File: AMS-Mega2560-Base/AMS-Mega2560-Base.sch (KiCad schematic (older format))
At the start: 18 parts, among them J23 RTD1, J24 RTD2, J25 Sense, J26 AdafruitUltimateGPS, J27 Sense, P1 Digital, P10 CONN_01X01, P11 CONN_01X01, P12 CONN_01X01, P13 CONN_01X01, P2 Power, P3 Analog, P4 Analog, P5 PWM, P6 PWM, P7 Communication, P8 CONN_01X01, P9 CONN_01X01

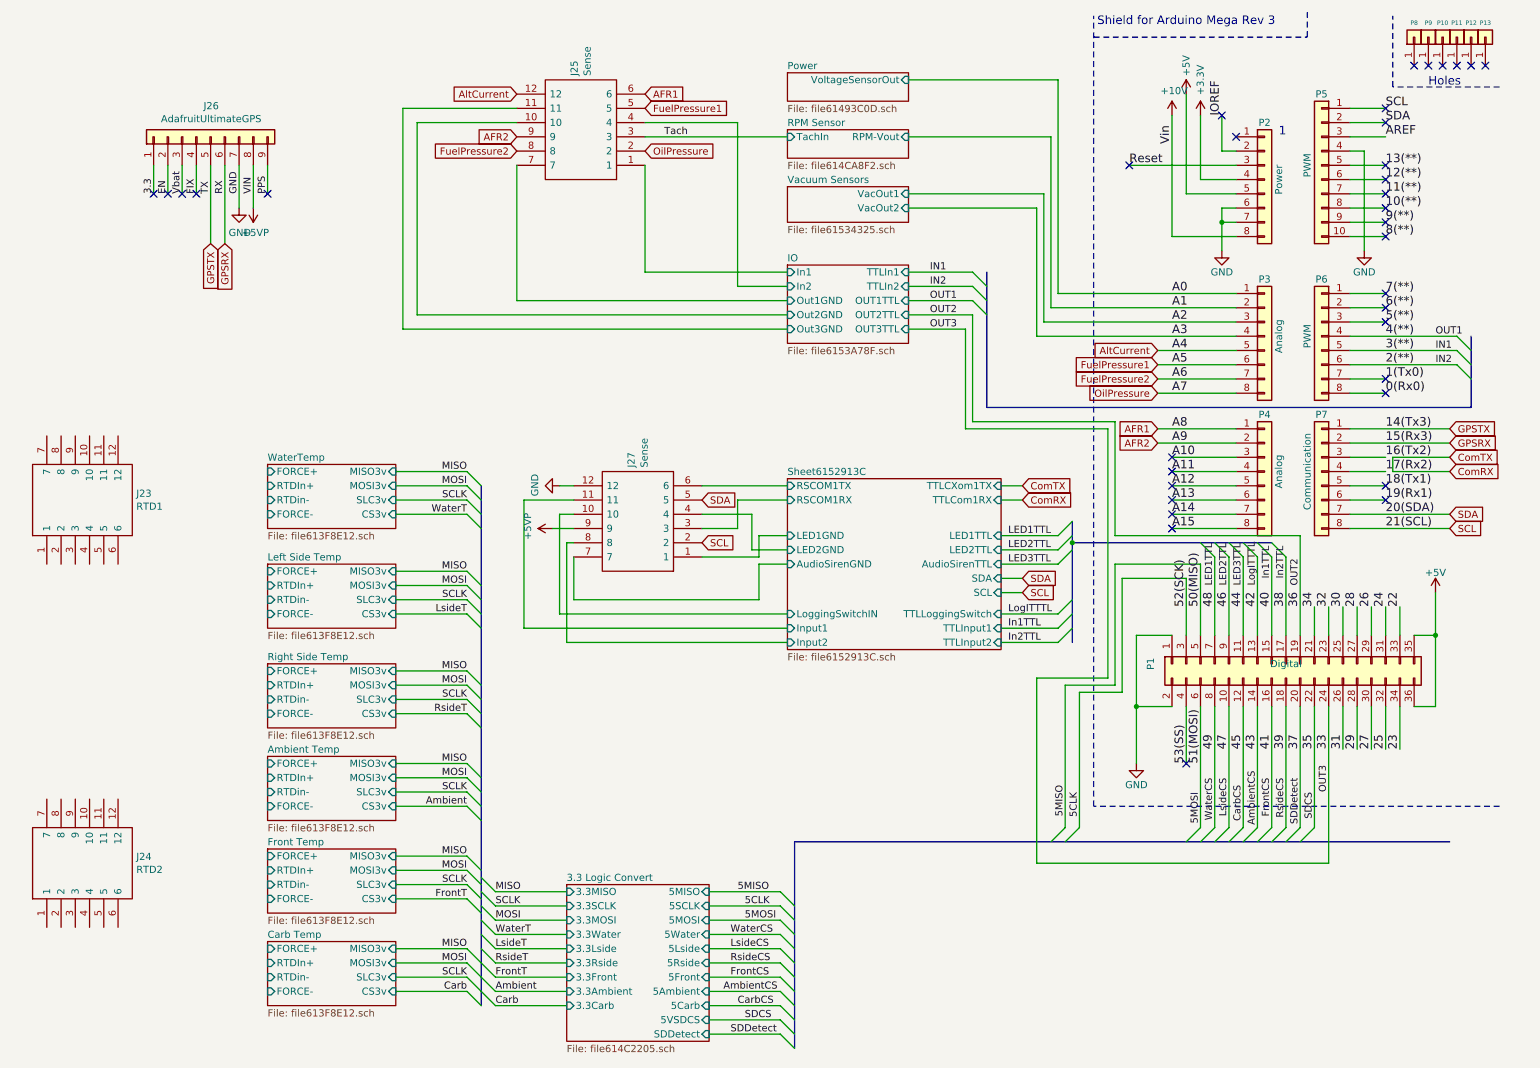
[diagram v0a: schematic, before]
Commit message: fixed the schematics for the RTC, IO and COMs. Realigned the RTD to screw term. need to finish the 3.3v portion of the power systems.
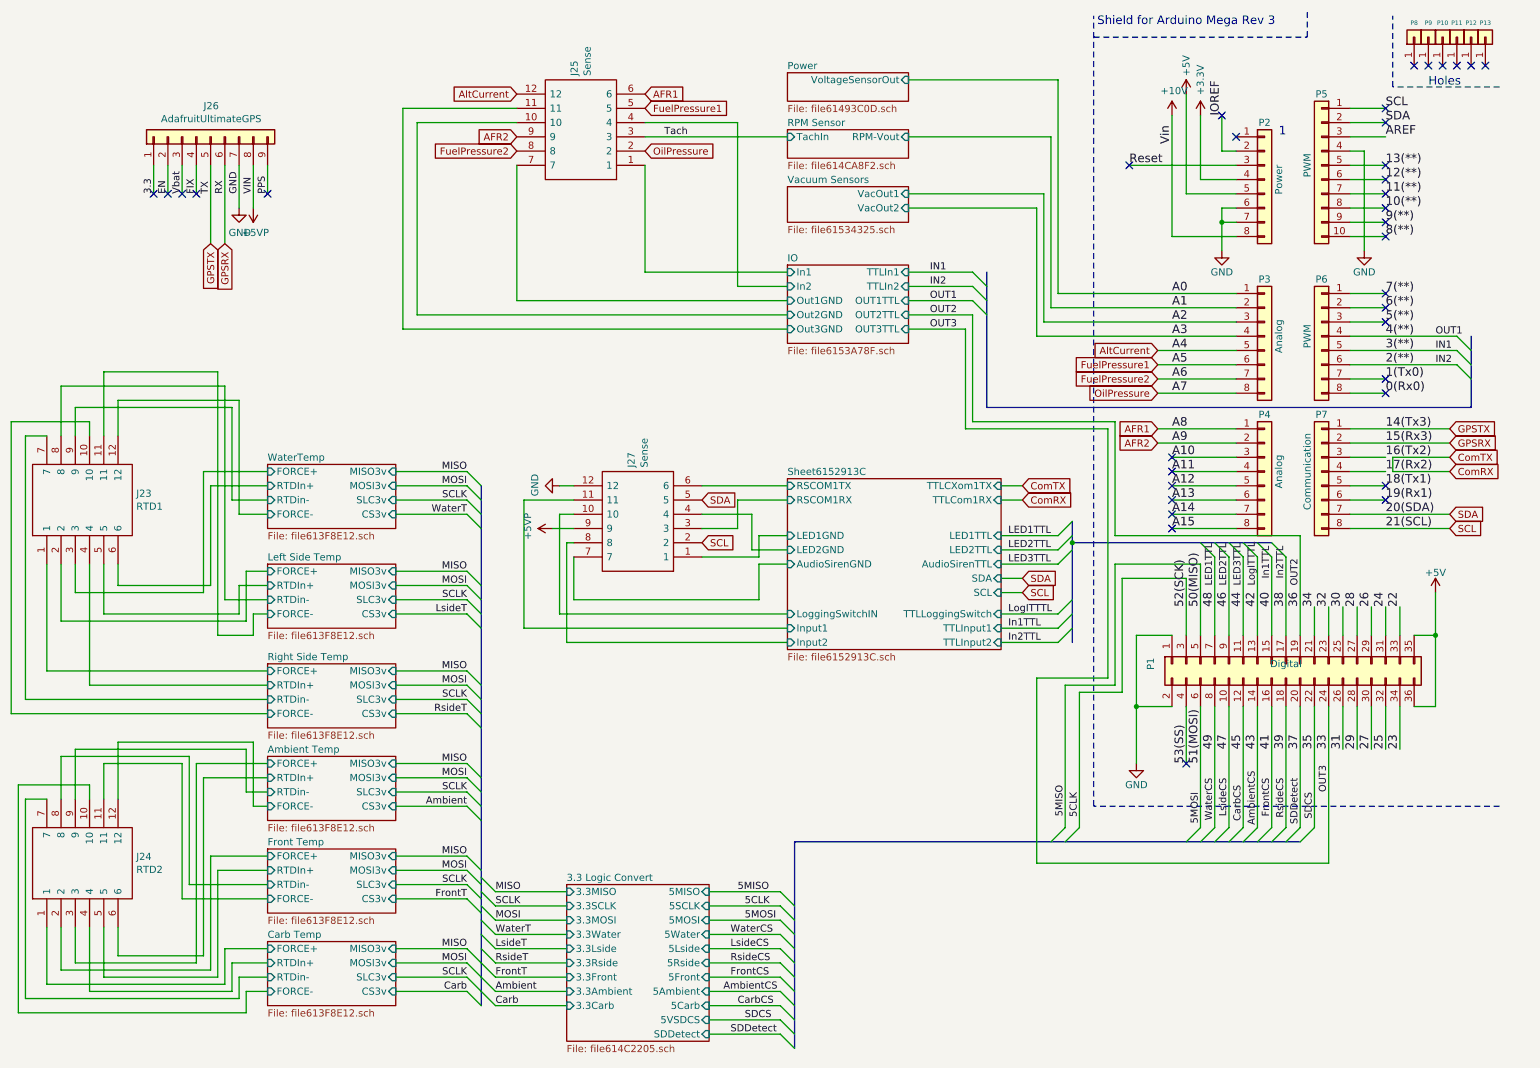
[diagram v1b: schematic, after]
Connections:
- net Ambient Temp/FORCE+: now also J24.3
- net Ambient Temp/FORCE-: now also J24.12
- net Ambient Temp/RTDIn+: now also J24.6
- net Ambient Temp/RTDin-: now also J24.9
- net Carb Temp/FORCE+: now also J24.1
- net Carb Temp/FORCE-: now also J24.10
- net Carb Temp/RTDIn+: now also J24.4
- net Carb Temp/RTDin-: now also J24.7
- net Front Temp/FORCE+: now also J24.2
- net Front Temp/FORCE-: now also J24.11
- net Front Temp/RTDIn+: now also J24.5
- net Front Temp/RTDin-: now also J24.8
- net Left Side Temp/FORCE+: now also J23.2
- net Left Side Temp/FORCE-: now also J23.11
- net Left Side Temp/RTDIn+: now also J23.5
- net Left Side Temp/RTDin-: now also J23.8
- net Right Side Temp/FORCE+: now also J23.1
- net Right Side Temp/FORCE-: now also J23.10
- net Right Side Temp/RTDIn+: now also J23.4
- net Right Side Temp/RTDin-: now also J23.7
- net WaterTemp/FORCE+: now also J23.3
- net WaterTemp/FORCE-: now also J23.12
- net WaterTemp/RTDIn+: now also J23.6
- net WaterTemp/RTDin-: now also J23.9
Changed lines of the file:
@@
 Text Label 10000 5950 1    50   ~ 0
 OUT3
-Wire Bus Line
-	8200 4050 8200 4200
-Wire Bus Line
-	11000 2750 11000 3250
-Wire Bus Line
-	7600 2300 7600 3250
-Wire Bus Line
-	8200 4200 8200 4900
-Wire Bus Line
-	8200 4200 9600 4200
-Wire Bus Line
-	6250 6300 6250 7750
-Wire Bus Line
-	6250 6300 10850 6300
-Wire Bus Line
-	4050 3800 4050 7450
 $Sheet
 S 6200 3750 1500 1200
@@
 F19 "LoggingSwitchIN" I L 6200 4700 50
 $EndSheet
+Wire Wire Line
+	2550 3700 2100 3700
+Wire Wire Line
+	2100 3700 2100 4550
+Wire Wire Line
+	2100 4550 1200 4550
+Wire Wire Line
+	1200 4550 1200 4350
+Wire Wire Line
+	2550 3800 2150 3800
+Wire Wire Line
+	2150 3800 2150 4500
+Wire Wire Line
+	2150 4500 1500 4500
+Wire Wire Line
+	1500 4500 1500 4350
+Wire Wire Line
+	2550 3900 2300 3900
+Wire Wire Line
+	2300 3250 1200 3250
+Wire Wire Line
+	1200 3250 1200 3450
+Wire Wire Line
+	2550 4000 2350 4000
+Wire Wire Line
+	2350 4000 2350 3200
+Wire Wire Line
+	2350 3200 1500 3200
+Wire Wire Line
+	1500 3200 1500 3450
+Wire Wire Line
+	2550 4400 2400 4400
+Wire Wire Line
+	2400 4400 2400 4750
+Wire Wire Line
+	2400 4750 1100 4750
+Wire Wire Line
+	1100 4750 1100 4350
+Wire Wire Line
+	2550 4500 2350 4500
+Wire Wire Line
+	2350 4500 2350 4700
+Wire Wire Line
+	1400 4700 1400 4350
+Wire Wire Line
+	2300 3900 2300 3250
+Wire Wire Line
+	1100 3450 1100 3100
+Wire Wire Line
+	1100 3100 2250 3100
+Wire Wire Line
+	2250 3100 2250 4600
+Wire Wire Line
+	2250 4600 2550 4600
+Wire Wire Line
+	2350 4700 1400 4700
+Wire Wire Line
+	2550 4700 2450 4700
+Wire Wire Line
+	2450 4700 2450 4850
+Wire Wire Line
+	2450 4850 2200 4850
+Wire Wire Line
+	2200 4850 2200 3000
+Wire Wire Line
+	2200 3000 1400 3000
+Wire Wire Line
+	1400 3000 1400 3450
+Wire Wire Line
+	2550 5100 1000 5100
+Wire Wire Line
+	1000 5100 1000 4350
+Wire Wire Line
+	2550 5200 1300 5200
+Wire Wire Line
+	1300 5200 1300 4350
+Wire Wire Line
+	2550 5300 850  5300
+Wire Wire Line
+	850  5300 850  3450
+Wire Wire Line
+	850  3450 1000 3450
+Wire Wire Line
+	1300 3450 1300 3350
+Wire Wire Line
+	1300 3350 750  3350
+Wire Wire Line
+	750  3350 750  5400
+Wire Wire Line
+	750  5400 2550 5400
+Wire Wire Line
+	1200 6900 1200 7150
+Wire Wire Line
+	1200 7150 2050 7150
+Wire Wire Line
+	2050 7150 2050 5750
+Wire Wire Line
+	2050 5750 2550 5750
+Wire Wire Line
+	2550 5850 2100 5850
+Wire Wire Line
+	2100 5850 2100 7100
+Wire Wire Line
+	2100 7100 1500 7100
+Wire Wire Line
+	1500 7100 1500 6900
+Wire Wire Line
+	1200 6000 1200 5650
+Wire Wire Line
+	1200 5650 2400 5650
+Wire Wire Line
+	2400 5650 2400 5950
+Wire Wire Line
+	2400 5950 2550 5950
+Wire Wire Line
+	1500 6000 1500 5600
+Wire Wire Line
+	1500 5600 2450 5600
+Wire Wire Line
+	2450 5600 2450 6050
+Wire Wire Line
+	2450 6050 2550 6050
+Wire Wire Line
+	2550 6400 2150 6400
+Wire Wire Line
+	2150 6400 2150 7200
+Wire Wire Line
+	2150 7200 1100 7200
+Wire Wire Line
+	1100 7200 1100 6900
+Wire Wire Line
+	1400 6900 1400 7250
+Wire Wire Line
+	1400 7250 2200 7250
+Wire Wire Line
+	2200 7250 2200 6500
+Wire Wire Line
+	2200 6500 2550 6500
+Wire Wire Line
+	1100 6000 1100 5700
+Wire Wire Line
+	1100 5700 2000 5700
+Wire Wire Line
+	2000 5700 2000 6600
+Wire Wire Line
+	2000 6600 2550 6600
+Wire Wire Line
+	2550 6700 1950 6700
+Wire Wire Line
+	1950 6700 1950 5750
+Wire Wire Line
+	1950 5750 1400 5750
+Wire Wire Line
+	1400 5750 1400 6000
+Wire Wire Line
+	2550 7050 2250 7050
+Wire Wire Line
+	1000 7300 1000 6900
+Wire Wire Line
+	2250 7050 2250 7300
+Wire Wire Line
+	2250 7300 1000 7300
+Wire Wire Line
+	1300 6900 1300 7350
+Wire Wire Line
+	1300 7350 2300 7350
+Wire Wire Line
+	2300 7350 2300 7150
+Wire Wire Line
+	2300 7150 2550 7150
+Wire Wire Line
+	2550 7250 2350 7250
+Wire Wire Line
+	2350 7250 2350 7400
+Wire Wire Line
+	2350 7400 850  7400
+Wire Wire Line
+	850  7400 850  6000
+Wire Wire Line
+	850  6000 1000 6000
+Wire Wire Line
+	1300 6000 1300 5900
+Wire Wire Line
+	1300 5900 800  5900
+Wire Wire Line
+	800  5900 800  7500
+Wire Wire Line
+	800  7500 2400 7500
+Wire Wire Line
+	2400 7500 2400 7350
+Wire Wire Line
+	2400 7350 2550 7350
+Wire Bus Line
+	8200 4050 8200 4200
+Wire Bus Line
+	11000 2750 11000 3250
+Wire Bus Line
+	7600 2300 7600 3250
+Wire Bus Line
+	8200 4200 8200 4900
+Wire Bus Line
+	8200 4200 9600 4200
+Wire Bus Line
+	6250 6300 6250 7750
+Wire Bus Line
+	6250 6300 9800 6300
+Wire Bus Line
+	4050 3800 4050 7450
 $EndSCHEMATC

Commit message: rearranging some of the hw design before i rename the repo.
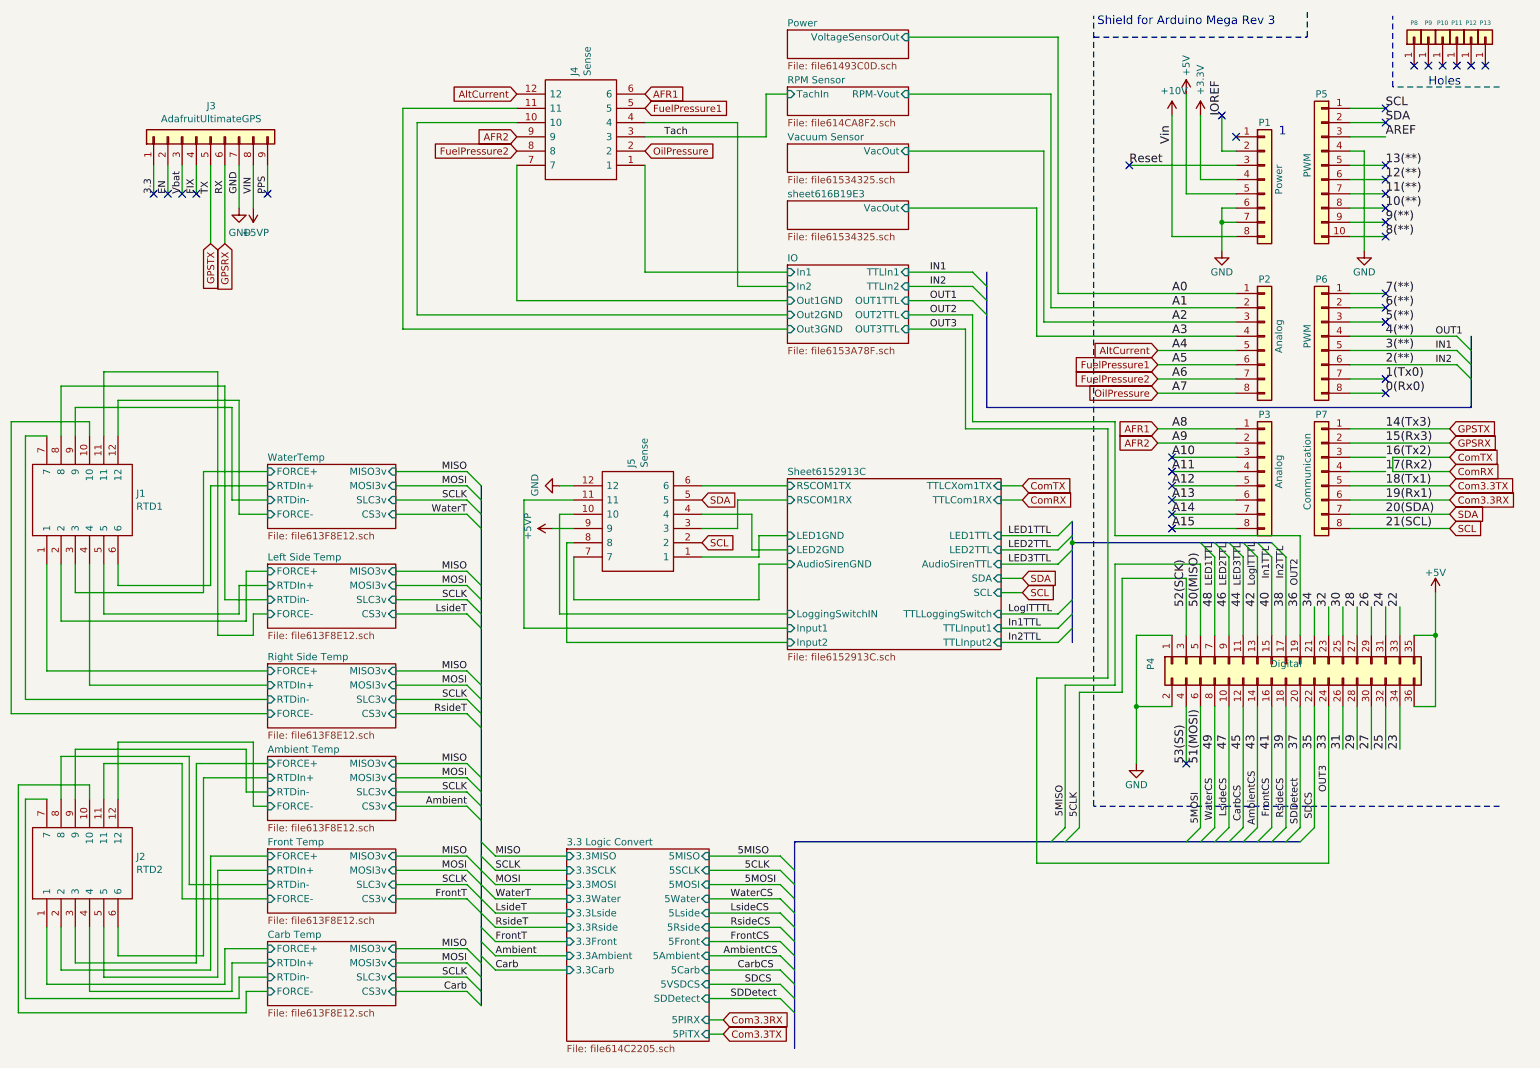
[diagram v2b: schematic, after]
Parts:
- renumbered J23 to J1, J24 to J2, J26 to J3, J25 to J4, J27 to J5, P2 to P1, P3 to P2, P4 to P3, P1 to P4
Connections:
- net 18(Tx1) renamed Com3.3TX
- net 19(Rx1) renamed Com3.3RX
- no-connect marks 36 -> 34
